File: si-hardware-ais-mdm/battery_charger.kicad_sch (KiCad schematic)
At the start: 16 parts, among them J1 CN1, J2 CN2, U2 MCP73811T-420I-OT

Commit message: schematic  to pcb
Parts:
- J1, J2: footprint Connector:JWT_A3963_1x02_P3.96mm_Vertical -> Connector_Stocko:Stocko_MKS_1652-6-0-202_1x2_P2.50mm_Vertical
- JP1: footprint (none) -> Jumper:SolderJumper-2_P1.3mm_Open_Pad1.0x1.5mm
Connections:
- net V_BATT: now also C12.2, C13.2, C14.2, J1.1 (Pin_1), J2.1 (Pin_1), U2.3 (V_{BAT})
- net GND: now reaches D3.1 (K)
- net GND: now also C10.1, C11.1, C12.1, C13.1, C14.1, C9.1, J1.2 (Pin_2), J2.2 (Pin_2), R7.1, R8.1, U2.2 (V_{SS})
- net at D3.2 (A): now also R5.1
- net at R8.2: now also JP1.1 (A)
- net VD: now reaches C11.2
- net VD: now also C10.2, C9.2, R6.1, U2.4 (V_{DD})
- net at R6.2: now also D4.2 (A)
- net at JP1.2 (B): now also R7.2, U2.5 (PROG)
- net at R5.2: now also D4.1 (K), U2.1 (CE)
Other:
- moved on the sheet: C12, C13, C14, J1, J2

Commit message: added chip flash 24LC64
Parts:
- R5, R6: footprint CTS_Resistor_SMD:R_0805_2012Metric -> CTS_Resistor_SMD:R_0603_1608Metric
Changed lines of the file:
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@@
 			)
 		)
-		(property "Footprint" "CTS_Resistor_SMD:R_0805_2012Metric"
+		(property "Footprint" "CTS_Resistor_SMD:R_0603_1608Metric"
 			(at 81.28 88.138 90)
 			(effects
@@
 			)
 		)
-		(property "Footprint" "CTS_Resistor_SMD:R_0805_2012Metric"
+		(property "Footprint" "CTS_Resistor_SMD:R_0603_1608Metric"
 			(at 99.06 79.248 90)
 			(effects

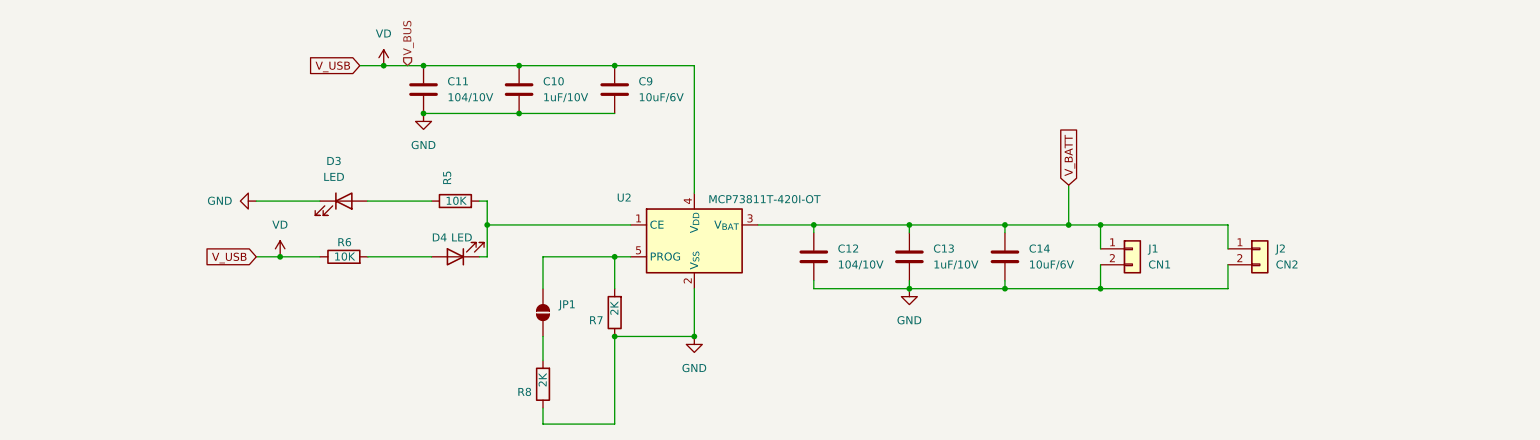
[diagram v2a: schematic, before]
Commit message: added ic charger
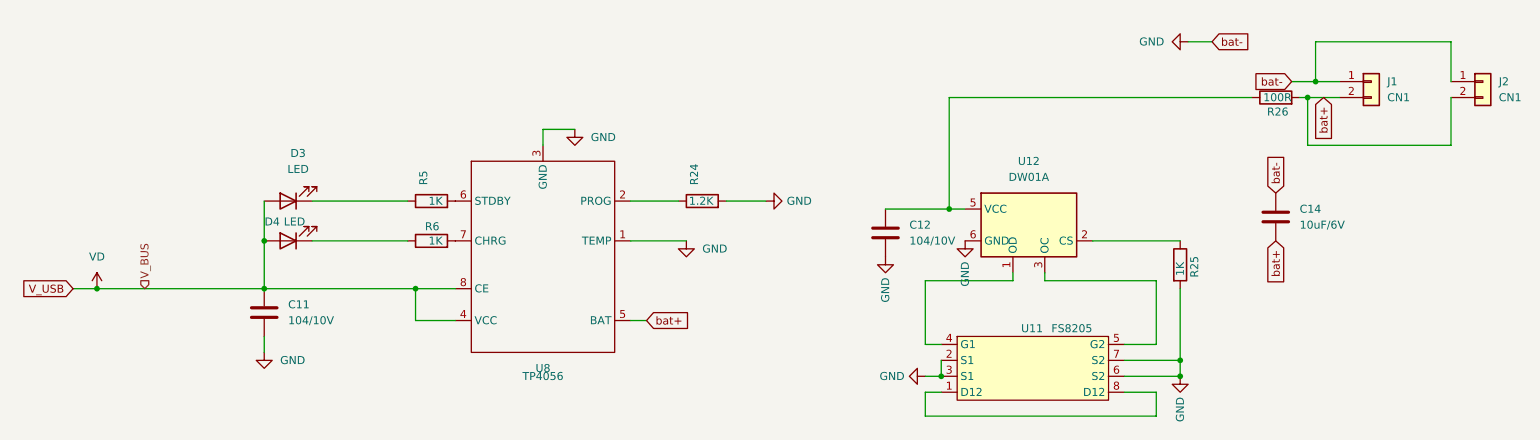
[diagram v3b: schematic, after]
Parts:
- removed C10, C13: 1uF/10V, CTS_Capacitor_SMD:C_0603_1608Metric, symbol Device:C
- removed C9: 10uF/6V, CTS_Capacitor_SMD:C_0603_1608Metric, symbol Device:C
- removed JP1: SolderJumper_2_Open, Jumper:SolderJumper-2_P1.3mm_Open_Pad1.0x1.5mm, symbol Jumper:SolderJumper_2_Open
- removed R7, R8: 2K, CTS_Resistor_SMD:R_0805_2012Metric, symbol Device:R
- removed U2: MCP73811T-420I-OT, Package_TO_SOT_SMD:SOT-23-5, symbol Battery_Management:MCP73811T-420I-OT
- added R24: 1.2K, CTS_Resistor_SMD:R_0603_1608Metric, symbol Device:R
- added R25: 1K, CTS_Resistor_SMD:R_0603_1608Metric, symbol Device:R
- added R26: 100R, CTS_Resistor_SMD:R_0603_1608Metric, symbol Device:R
- added U11: FS8205, Package_SO:TSSOP-8_4.4x3mm_P0.65mm, symbol ST_Mosfet:FS8205
- added U12: DW01A, Package_TO_SOT_SMD:SOT-23-6, symbol Battery_Management:DW01A
- added U8: TP4056, Package_SO:SOP-8_3.9x4.9mm_P1.27mm, symbol SI_Bat_Managerment:TP4056
- J2: value CN2 -> CN1
- R5, R6: value 10K -> 1K
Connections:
- net GND: now also C14.2, J1.1 (Pin_1), J2.1 (Pin_1), R24.2, R25.2, U11.2 (S1), U11.3 (S1), U11.6 (S2), U11.7 (S2), U12.6 (GND), U8.1 (TEMP), U8.3 (GND); no longer C14.1, D3.1 (K), J1.2 (Pin_2), J2.2 (Pin_2)
- net VD: now also D3.2 (A), D4.2 (A), U8.4 (VCC), U8.8 (CE); no longer R6.1
- net at R5.1: now also D3.1 (K); no longer D3.2 (A)
- net at R6.2: now also U8.7 (CHRG); no longer D4.2 (A)
- net at R5.2: now also U8.6 (STDBY); no longer D4.1 (K)
- removed net V_BATT: C12.2, C14.2, J1.1 (Pin_1), J2.1 (Pin_1)
- new net: U11.1 (D12), U11.8 (D12)
- new net: U11.4 (G1), U12.1 (OD)
- new net: U11.5 (G2), U12.3 (OC)
- new net: R24.1, U8.2 (PROG)
- new net: D4.1 (K), R6.1
- new net: C12.2, R26.1, U12.5 (VCC)
- new net: R25.1, U12.2 (CS)
- new net bat+: C14.1, J1.2 (Pin_2), J2.2 (Pin_2), R26.2, U8.5 (BAT)
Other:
- moved on the sheet: D3, D4, R5, R6
